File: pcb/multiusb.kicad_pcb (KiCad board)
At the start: 2 copper layers, 11 parts, among them P1 USB_MICRO_OTG, P2 USB_MINI_OTG, P3 USB_A

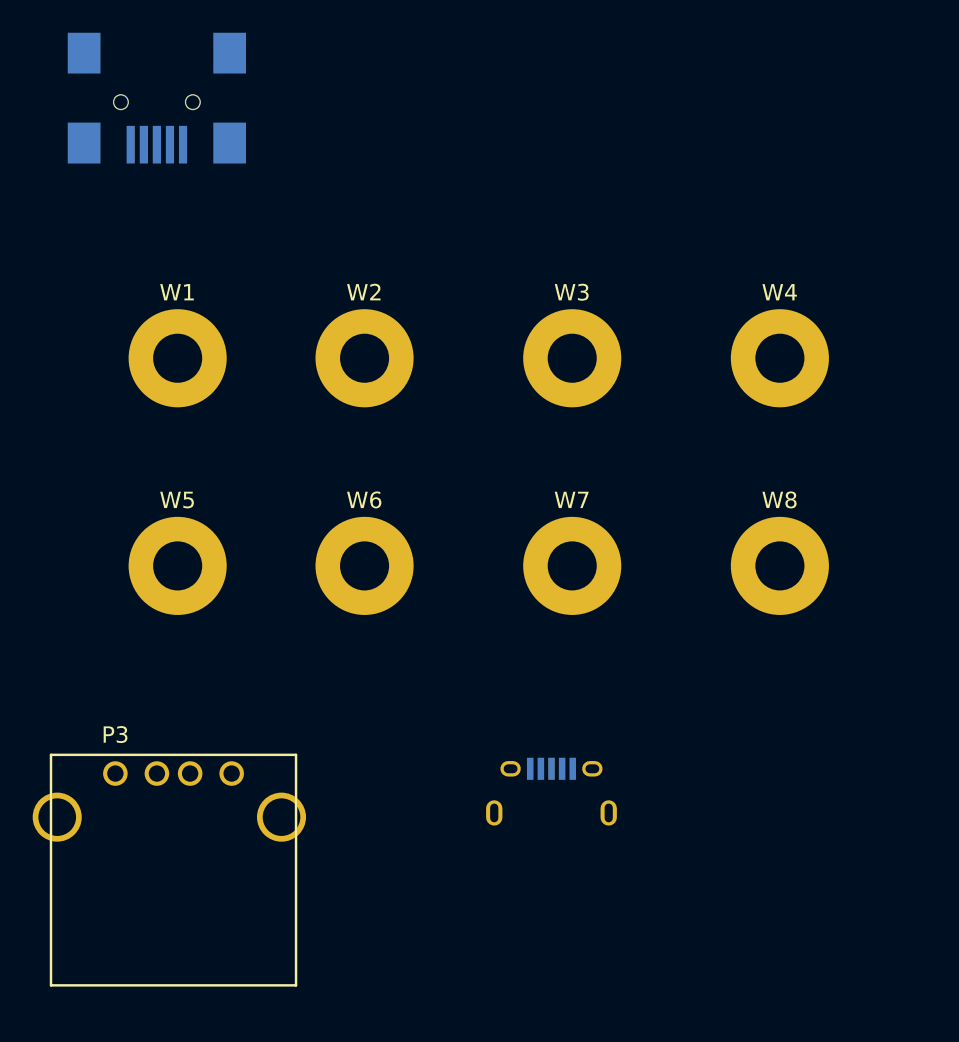
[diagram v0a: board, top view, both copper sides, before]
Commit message: updated USB A footprint
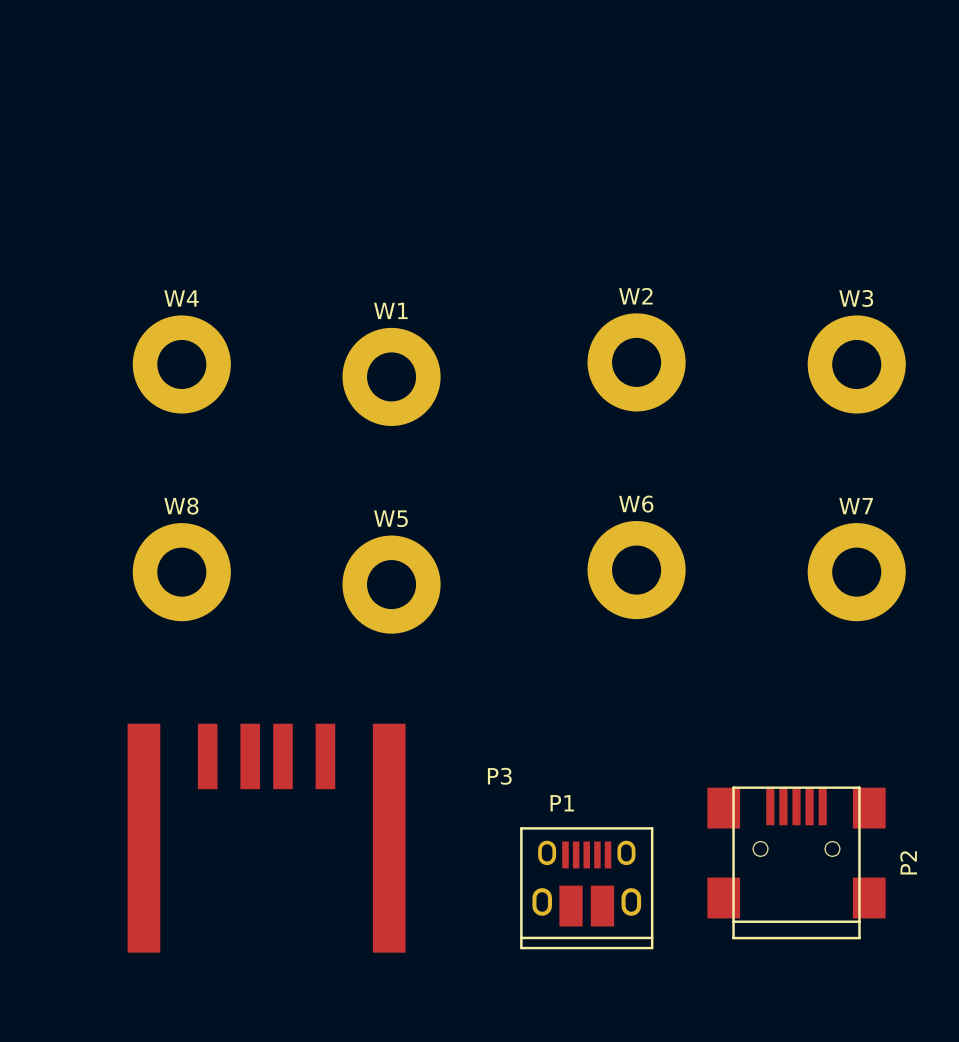
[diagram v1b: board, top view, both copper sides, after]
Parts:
- P1: footprint Connectors:USB_Micro-B -> Connectors:USB_Micro-B_10103594-0001LF; moved to F.Cu
- P2: moved to F.Cu
- P3: footprint Connectors:USB_A -> project:USB_A
- moved P2 61.4 mm to (162.3, 132.5), turned to 90 degrees
- moved W4 36.6 mm to (124.7, 102.0)
- moved W8 36.6 mm to (124.7, 114.7)
- moved W3 17.4 mm to (166.0, 102.0)
- moved W7 17.4 mm to (166.0, 114.7)
- moved W2 16.6 mm to (152.5, 101.9)
- moved W6 16.6 mm to (152.5, 114.6)
- moved P3 16.0 mm to (136.4, 124.0), turned to 180 degrees
- moved W1 13.1 mm to (137.5, 102.7)
- moved W5 13.1 mm to (137.5, 115.4)
- moved P1 5.64 mm to (149.5, 133.5), turned to 0 degrees

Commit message: getting close to the final pcb layout
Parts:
- removed W1, W2, W3, W4, W5, W6, W7, W8: TEST_1P, Mounting_Holes:MountingHole_3mm_Pad
- moved P2 17.3 mm to (146.7, 125.1), turned to 270 degrees
- moved P1 3.94 mm to (148.1, 137.2)
- moved P3 3.41 mm to (134.7, 126.9)
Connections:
- P1 pad 4: Net-(P1-Pad4) -> (no net)
- P2 pad 4: Net-(P2-Pad4) -> (no net)
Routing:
- net /D+: track 0.00 -> 54.1 mm
- net /D-: track 0.00 -> 44.2 mm
- net /VCC: track 0.00 -> 31.2 mm
- net /GND: track 0.00 -> 4.07 mm
- added copper zone on F.Cu, net /GND

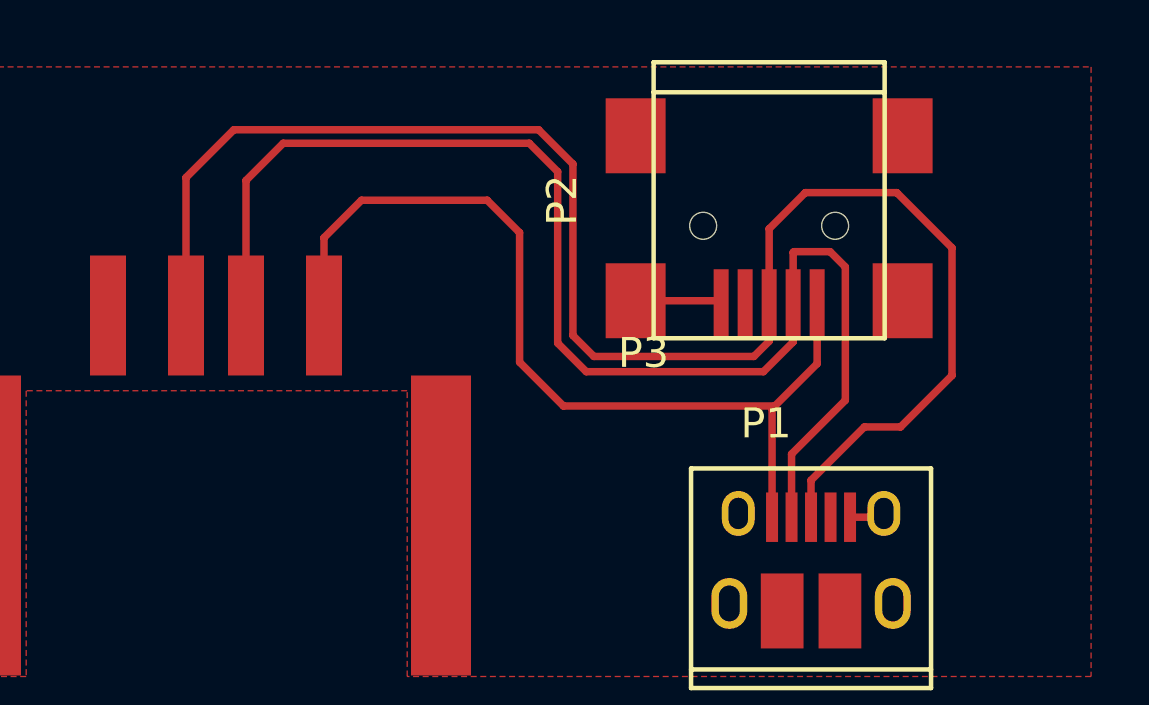
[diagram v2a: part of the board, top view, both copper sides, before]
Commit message: wider tracks, push and shove tool test
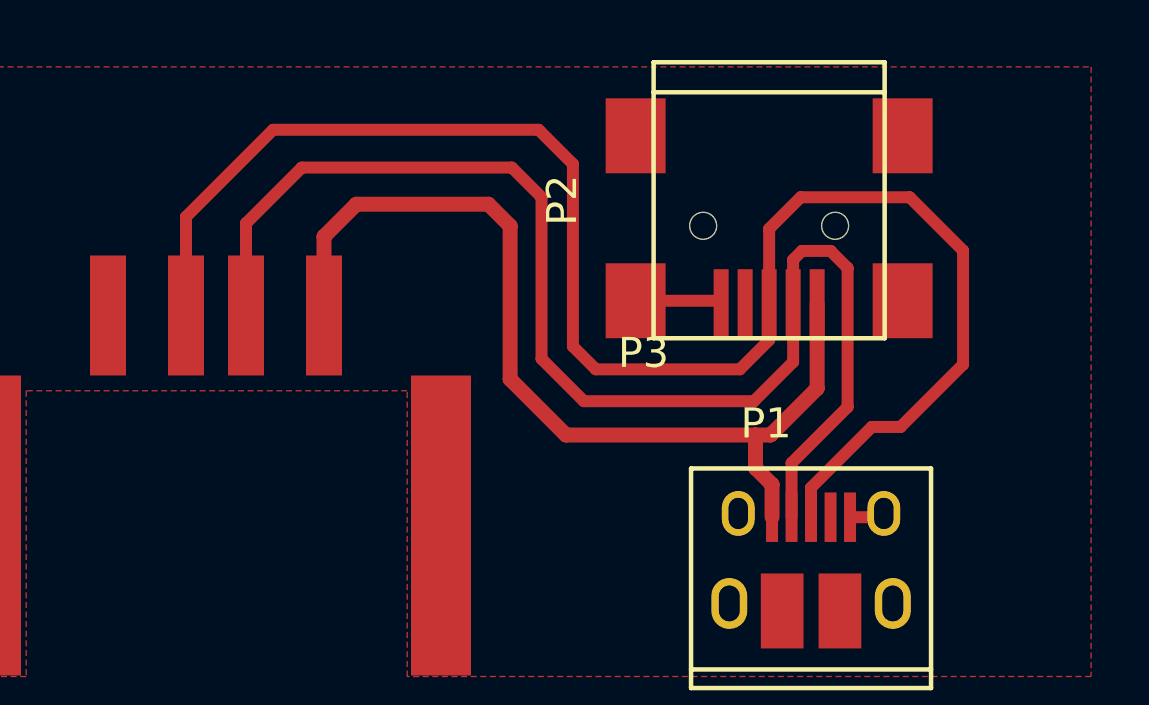
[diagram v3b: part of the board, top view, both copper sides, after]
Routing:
- net /VCC: track 31.2 -> 32.1 mm
- net /D-: track 44.2 -> 43.7 mm
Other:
- net class +5v added: clearance 0.2, trace_width 0.5, via_dia 0.6, via_drill 0.4
- net class Default: trace_width 0.25 -> 0.4
